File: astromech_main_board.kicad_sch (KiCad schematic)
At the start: 75 parts, among them IC1 MAX11645EUA+, J1 Conn_01x03, J10 61201621621, J11 Conn_01x06, J15 Conn_01x04, J18 Screw_Terminal_01x10, J19 Conn_01x04, J2 Conn_02x03_Odd_Even, J20 Conn_01x04, J21 Conn_01x04, J3 Conn_01x03, J4 IO_XPAND, J7 Conn_01x03, J8 Conn_01x03, J9 Conn_01x06, Q1 2N7002, U10 LS7366R, U11 LS7366R, U3 NCP1117-3.3_SOT223, U4 NCP1117-5.0_TO252, U5 SC16IS752IPW_128, U6 PCF8575PWR, U7 TCA9517ADGK, U8 74HC14, U9 LS7366R, Y1 8MHz, Y2 Crystal

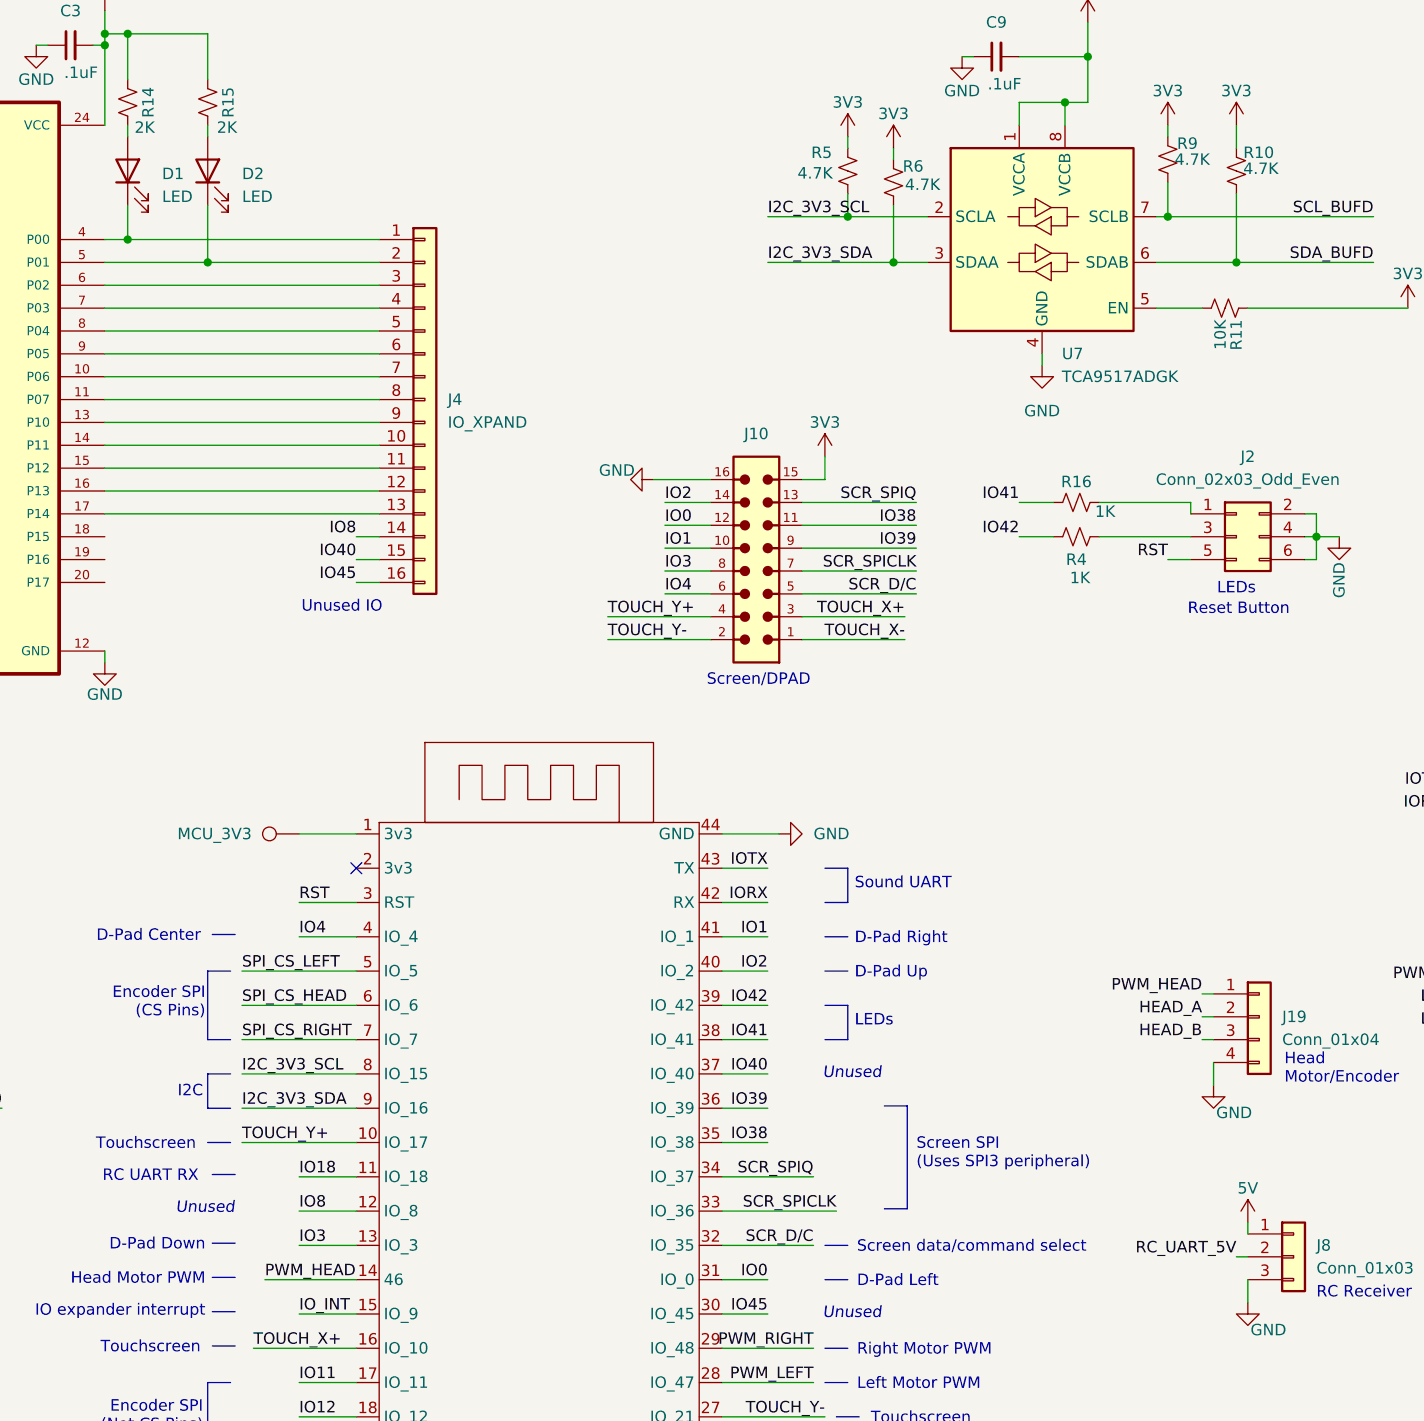
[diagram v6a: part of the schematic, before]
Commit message: fixed pinout and some silkscreen labels
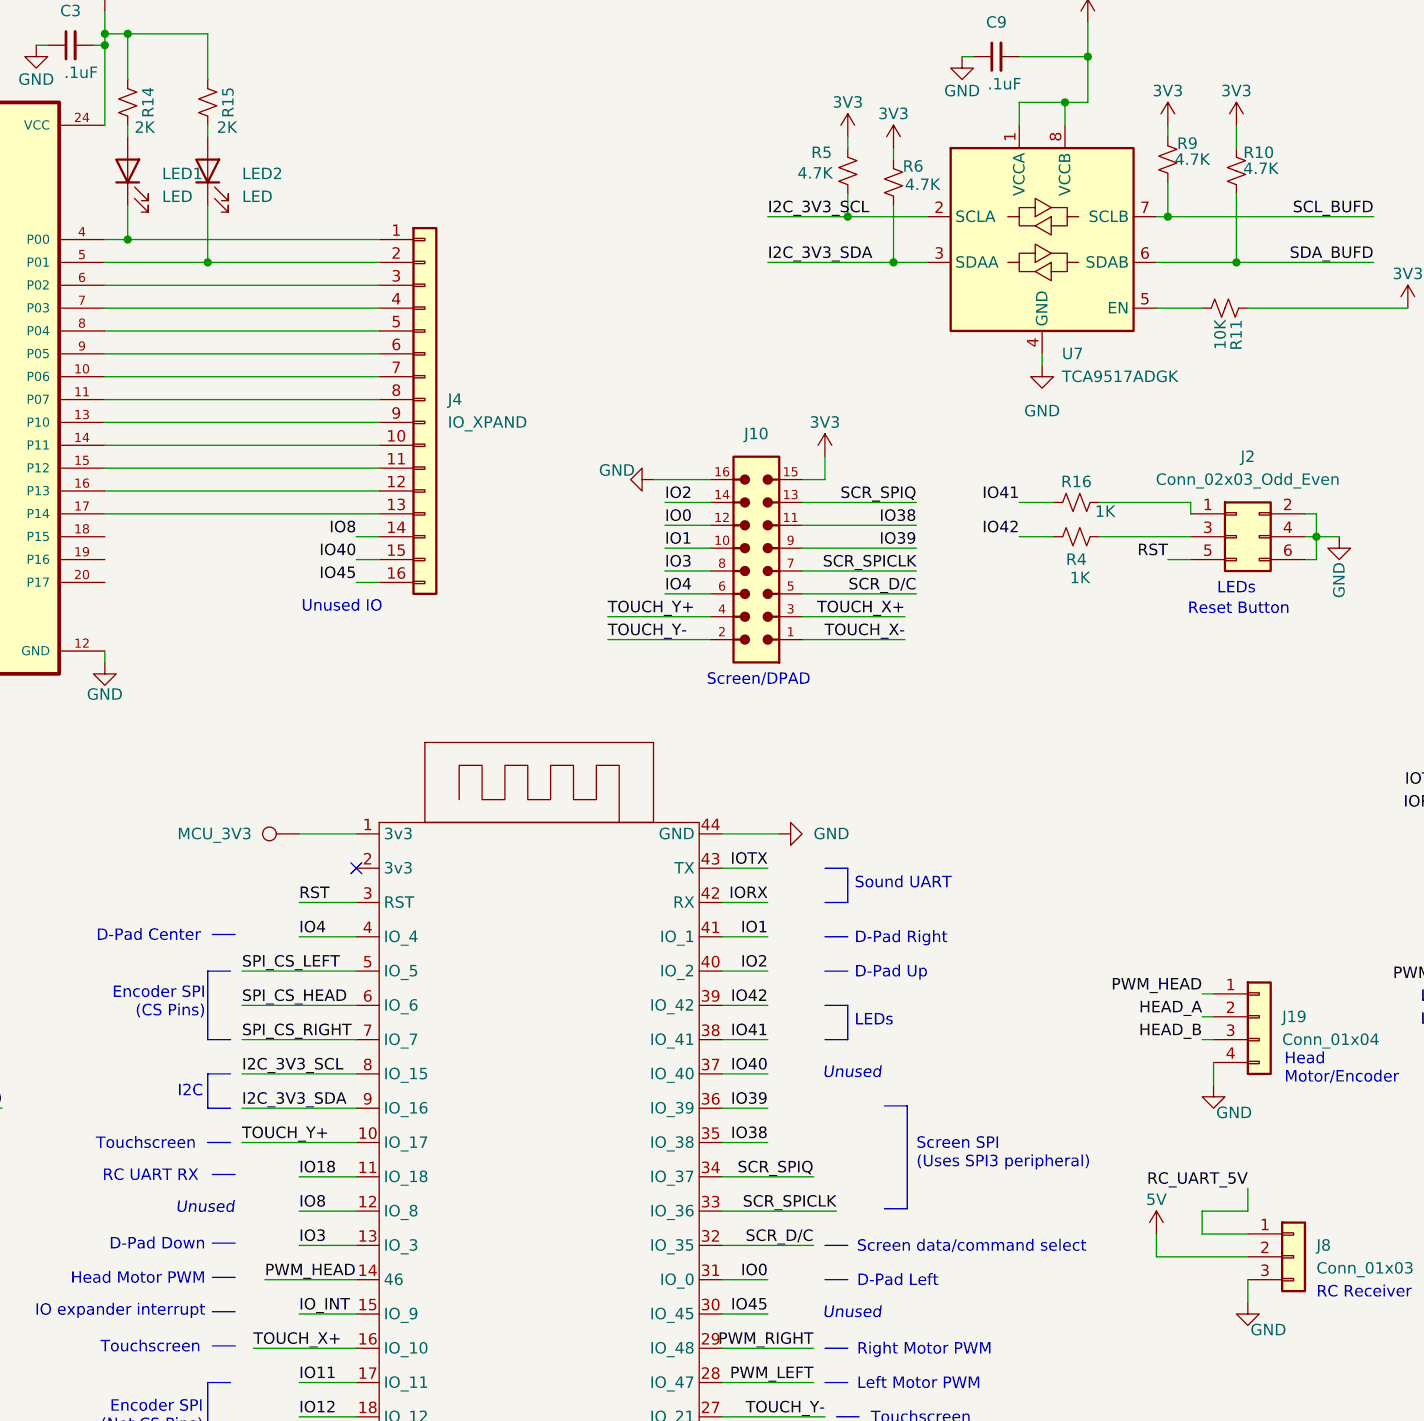
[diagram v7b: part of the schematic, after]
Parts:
- renumbered D1 to LED1, D2 to LED2
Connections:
- net 5V: now also J8.2 (Pin_2); no longer J8.1 (Pin_1)
- net RC_UART_5V: now also J8.1 (Pin_1); no longer J8.2 (Pin_2)

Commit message: added diode
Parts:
- added D1: MBR1020VL, Diode_SMD:D_SOD-123F, symbol Diode:MBR1020VL
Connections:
- net 5V: now also D1.2 (A); no longer U13.21 (5Vin)
- new net: D1.1 (K), U13.21 (5Vin)
- no-connect marks 39 -> 42
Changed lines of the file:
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@@
 	)
 	(no_connect
+		(at 62.23 184.15)
+	)
+	(no_connect
 		(at 90.17 218.44)
 	)
@@
 	)
 	(no_connect
+		(at 62.23 181.61)
+	)
+	(no_connect
 		(at 111.76 74.93)
 	)
@@
 	)
 	(no_connect
+		(at 62.23 186.69)
+	)
+	(no_connect
 		(at -31.75 105.41)
 	)
@@
 		)
 	)
+	(wire
+		(pts
+			(xy 46.99 294.64) (xy 59.69 294.64)
+		)
+		(stroke
+			(width 0)
+			(type default)
+		)
+	)
 	(polyline
 		(pts
@@
 	(wire
 		(pts
+			(xy 81.28 290.83) (xy 90.17 290.83)
+		)
+		(stroke
+			(width 0)
+			(type default)
+		)
+	)
+	(wire
+		(pts
+			(xy 67.31 294.64) (xy 81.28 294.64)
+		)
+		(stroke
+			(width 0)
+			(type default)
+		)
+	)
+	(wire
+		(pts
 			(xy 63.5 31.75) (xy 63.5 35.56)
 		)
@@
 	(wire
 		(pts
-			(xy 46.99 285.75) (xy 46.99 290.83)
+			(xy 46.99 285.75) (xy 46.99 294.64)
 		)
 		(stroke
@@
 	(wire
 		(pts
-			(xy 46.99 290.83) (xy 90.17 290.83)
-		)
-		(stroke
-			(width 0)
-			(type default)
-		)
-	)
-	(wire
-		(pts
 			(xy 187.96 151.13) (xy 203.2 151.13)
 		)
@@
 	(wire
 		(pts
+			(xy 81.28 294.64) (xy 81.28 290.83)
+		)
+		(stroke
+			(width 0)
+			(type default)
+		)
+	)
+	(wire
+		(pts
 			(xy 83.82 275.59) (xy 90.17 275.59)
 		)
@@
 					(unit 1)
 				)
+			)
+		)
+	)
+	(symbol
+		(lib_id "Diode:MBR1020VL")
+		(at 63.5 294.64 180)
+		(unit 1)
+		(exclude_from_sim no)
+		(in_bom yes)
+		(on_board yes)
+		(dnp no)
+		(fields_autoplaced yes)
+		(property "Reference" "D1"
+			(at 63.8175 288.29 0)
+			(effects
+				(font
+					(size 1.27 1.27)
+				)
+			)
+		)
+		(property "Value" "MBR1020VL"
+			(at 63.8175 290.83 0)
+			(effects
+				(font
+					(size 1.27 1.27)
+				)
+			)
+		)
+		(property "Footprint" "Diode_SMD:D_SOD-123F"
+			(at 63.5 290.195 0)
+			(effects
+				(font
+					(size 1.27 1.27)
+				)
+				(hide yes)
+			)
+		)
+		(property "Datasheet" "https://www.onsemi.com/pub/Collateral/MBR1020VL-D.PDF"
+			(at 63.5 294.64 0)
+			(effects
+				(font
+					(size 1.27 1.27)
+				)
+				(hide yes)
+			)
+		)
+		(property "Description" "20V, 1A, 340 mV, Schottky Diode Rectifier, SOD-123F"
+			(at 63.5 294.64 0)
+			(effects
+				(font
+					(size 1.27 1.27)
+				)
+				(hide yes)
+			)
+		)
+		(pin "1"
+		)
+		(pin "2"
+		)
+		(instances
+			(project ""
+				(path "/3ed70c37-1dc6-4761-9813-fca49ce12494"
+					(reference "D1")
+					(unit 1)
+				)
